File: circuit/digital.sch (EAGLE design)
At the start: 77 parts, among them IC1 OP07C, IC2 74HC4052D, IC3 AD8603UJ, IC4 AD8221R, IC5 AD8221R, IC6 LM258, IC7 LM258

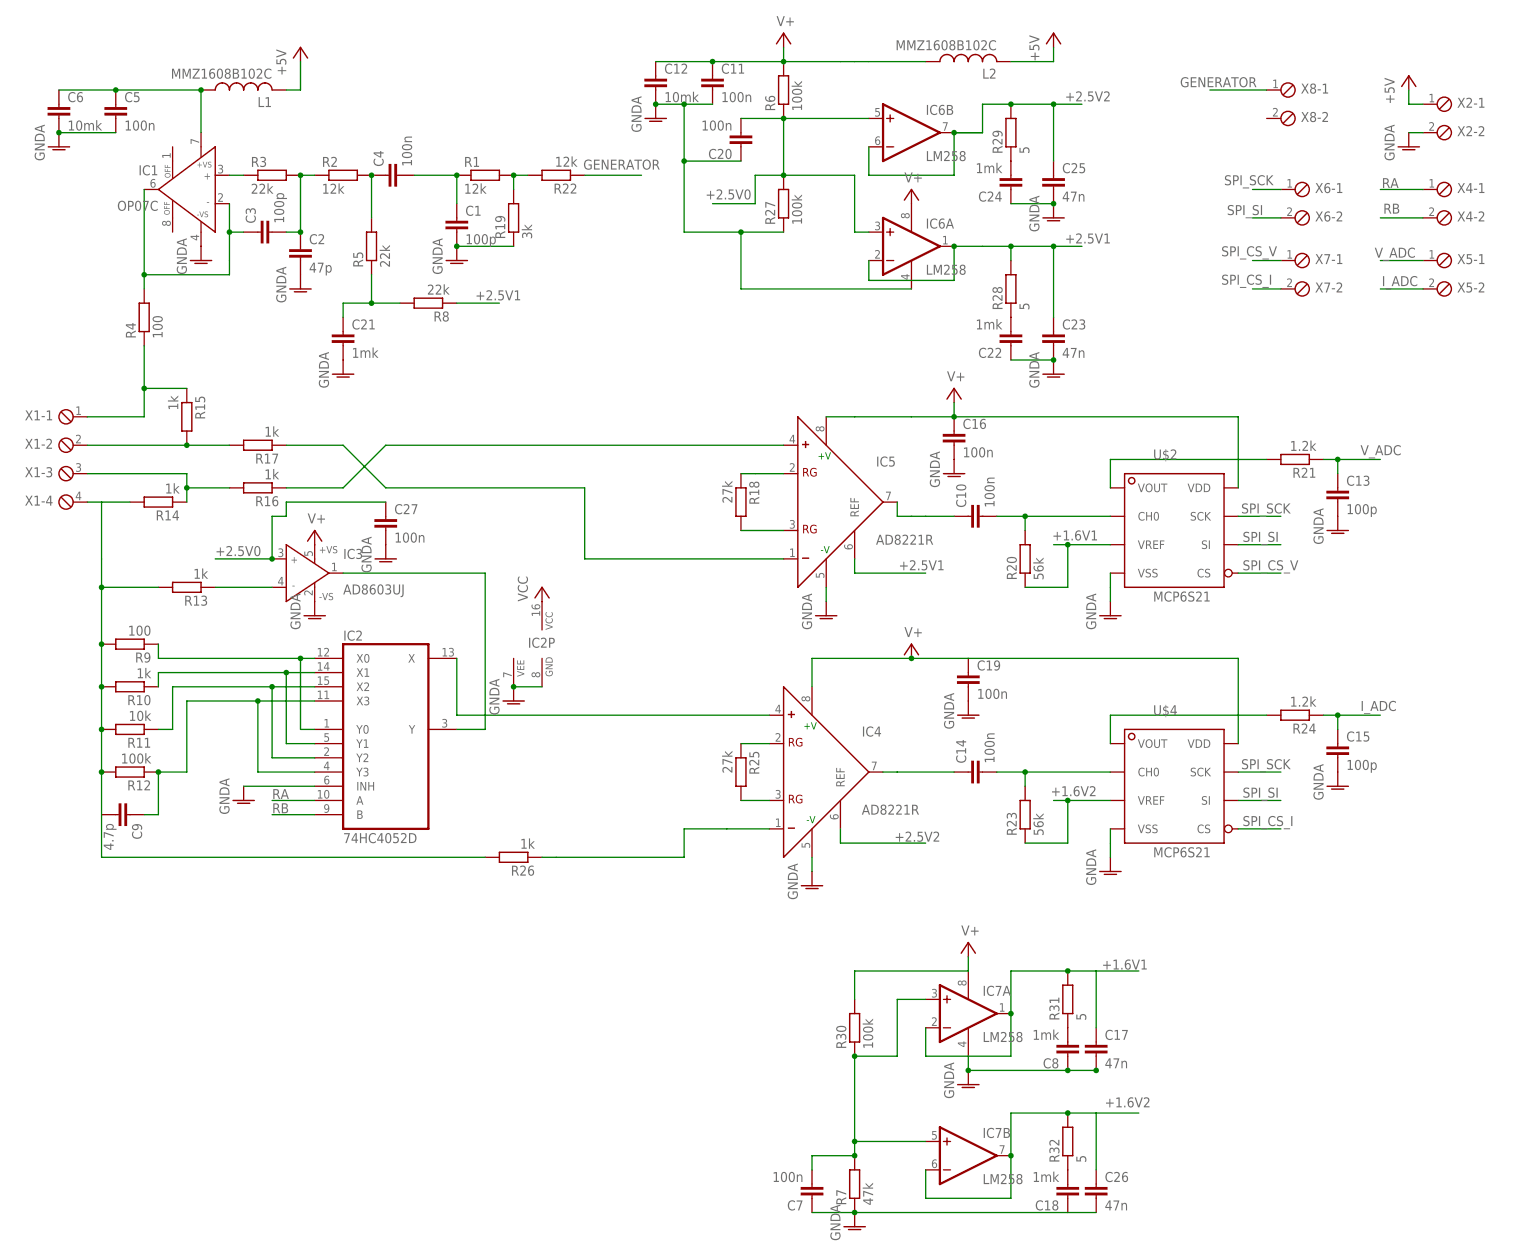
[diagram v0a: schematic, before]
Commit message: - начали делать цифровую часть
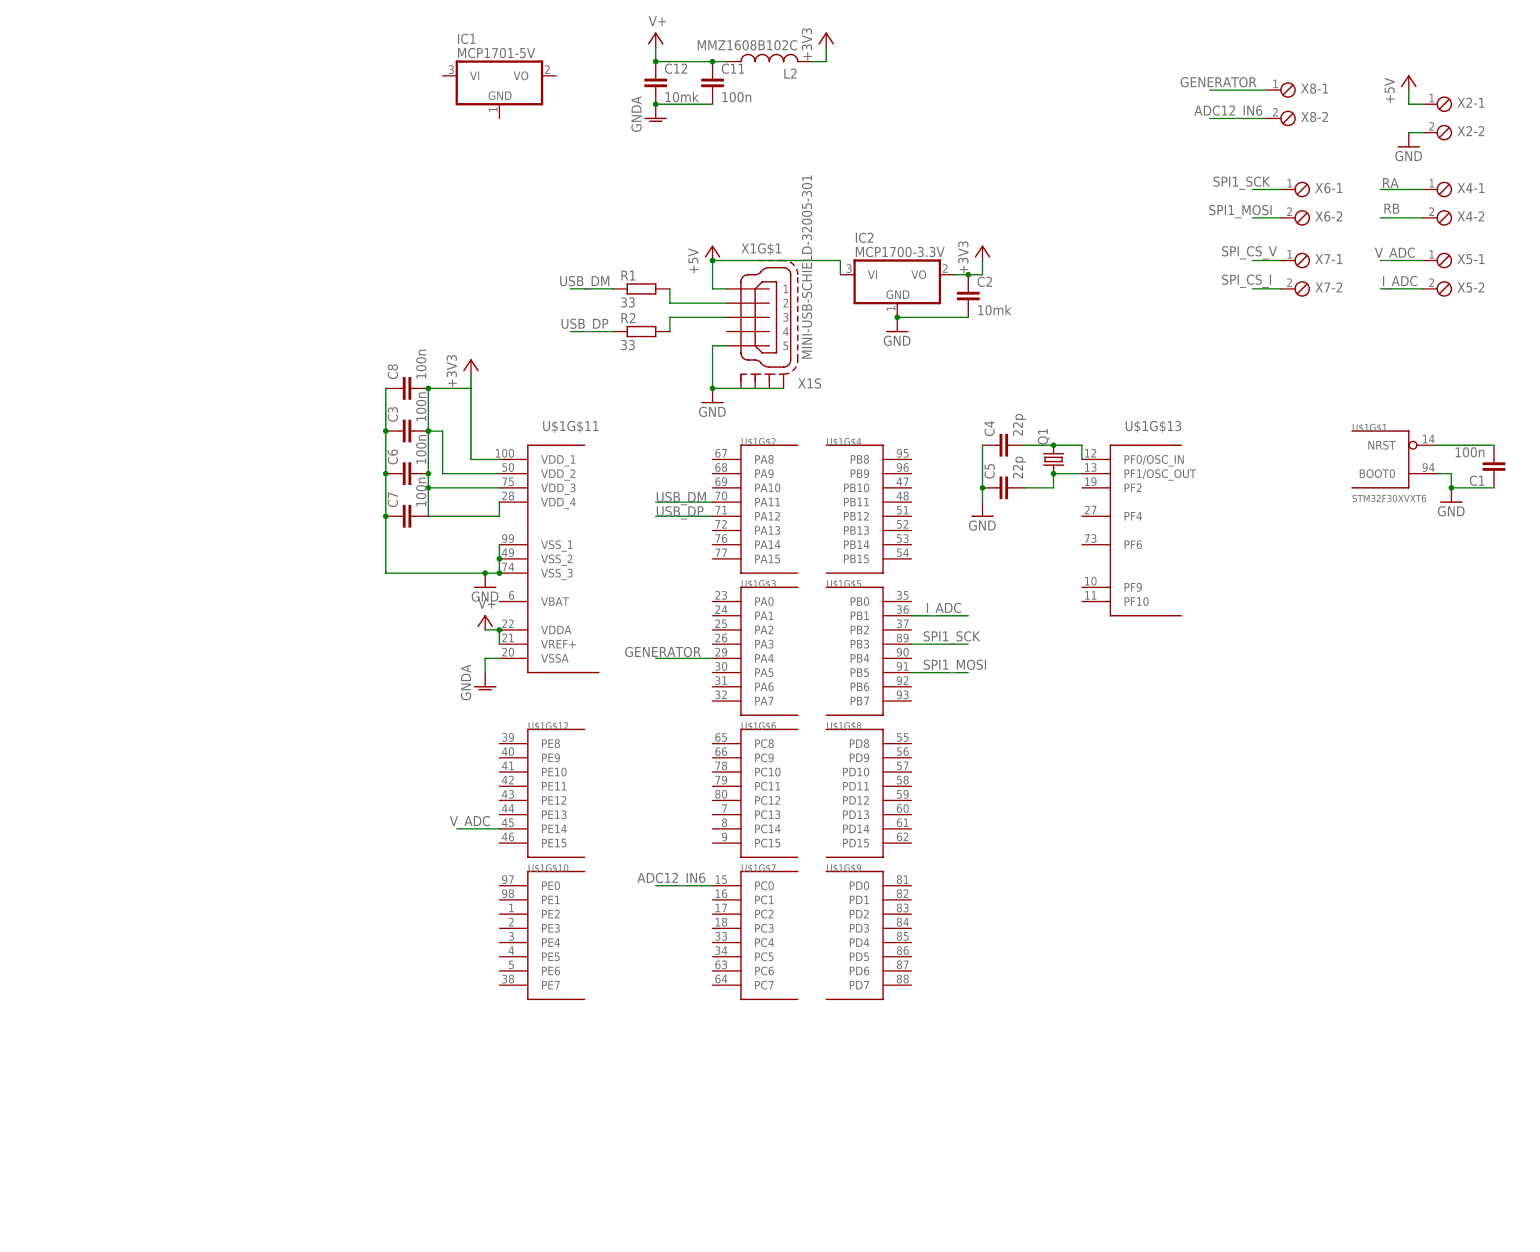
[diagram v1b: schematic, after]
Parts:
- removed C10, C14, C16, C19, C20, C27: 100n, rcl:C-EUC0603
- removed C13, C15: 100p, rcl:C-EUC0805
- removed C17, C23, C25, C26: 47n, rcl:C-EUC0805
- removed C18, C21, C22, C24: 1mk, rcl:C-EUC0603
- removed C9: 4.7p, rcl:C-EUC0805
- removed IC3: AD8603UJ, analog-devices:AD8603UJ
- removed IC4, IC5: AD8221R, balmer:AD8221R
- removed IC6, IC7: LM258, linear:LM358D
- removed L1: MMZ1608B102C, rcl:L-US
- removed R10, R13, R14, R15, R16, R17, R26: 1k, rcl:R-EU_R0603
- removed R11: 10k, rcl:R-EU_R0603
- removed R12, R27, R30, R6: 100k, rcl:R-EU_R0603
- removed R18, R25: 27k, rcl:R-EU_R0603
- removed R19: 3k, rcl:R-EU_R0603
- removed R20, R23: 56k, rcl:R-EU_R0603
- removed R21, R24: 1.2k, rcl:R-EU_R0603
- removed R22: 12k, rcl:R-EU_R0603
- removed R28, R29, R31, R32: 5, rcl:R-EU_R0805
- removed R3, R5, R8: 22k, rcl:R-EU_R0603
- removed R4, R9: 100, rcl:R-EU_R0603
- removed R7: 47k, rcl:R-EU_R0603
- removed U$2, U$4: MCP6S21, balmer:MCP6S21
- added Q1: (no value), crystal:CRYSTALHC49UP
- added U$1: STM32F30XVXT6, stm32:STM32F30XVXT6
- C1, C3: value 100p -> 100n; device rcl:C-EUC0805 -> rcl:C-EUC0603
- C2: value 47p -> 10mk
- C4, C5: value 100n -> 22p; device rcl:C-EUC0603 -> rcl:C-EUC0805
- C6: value 10mk -> 100n; device rcl:C-EUC0805 -> rcl:C-EUC0603
- C8: value 1mk -> 100n
- IC1: value OP07C -> MCP1701-5V; device analog-devices:AD817 -> linear:MCP1703CB
- IC2: value 74HC4052D -> MCP1700-3.3V; device 40xx:4052D -> linear:MCP1703CB
- L2: device rcl:L-US -> rcl:L-US0204/7
- R1, R2: value 12k -> 33
- X1: value (none) -> MINI-USB-SCHIELD-32005-301; device con-phoenix-254:MPT4 -> con-cypressindustries:MINI-USB-SCHIELD-32005-301
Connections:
- removed net +1.6V1: C17.1, IC7A.-IN, IC7A.OUT, R20.1, R31.2, U$2.VREF
- removed net +1.6V2: C26.1, IC7B.-IN, IC7B.OUT, R23.1, R32.2, U$4.VREF
- removed net +2.5V0: C20.2, C27.1, IC3.IN+, IC6A.+IN, IC6B.+IN, R27.2, R6.1
- removed net +2.5V1: C23.1, IC5.REF, IC6A.-IN, IC6A.OUT, R28.2, R8.1
- removed net +2.5V2: C25.1, IC4.REF, IC6B.-IN, IC6B.OUT, R29.2
- removed net N$10: C21.1, R5.1, R8.2
- removed net N$11: IC2A.Y, IC3.OUT
- removed net N$12: IC2A.X0, IC2A.Y0, R9.1
- removed net N$13: IC2A.X1, IC2A.Y1, R10.1
- removed net N$14: IC2A.X2, IC2A.Y2, R11.1
- removed net N$15: C9.1, IC2A.X3, IC2A.Y3, R12.1
- removed net N$16: R14.1, R16.2, X1-3.1
- removed net N$17: R15.2, R17.2, X1-2.1
- removed net N$18: C9.2, R10.2, R11.2, R12.2, R13.2, R14.2, R26.2, R9.2, X1-4.1
- removed net N$19: R15.1, R4.1, X1-1.1
- removed net N$20: C10.1, IC5.OUT
- removed net N$21: IC4.RG@1, R25.1
- removed net N$22: IC4.-, R26.1
- removed net N$23: IC5.RG@2, R18.2
- removed net N$24: IC5.RG@1, R18.1
- removed net N$25: C14.2, R23.2, U$4.CH0
- removed net N$26: R24.2, U$4.VOUT
- removed net N$27: C10.2, R20.2, U$2.CH0
- removed net N$28: R21.2, U$2.VOUT
- removed net N$29: C14.1, IC4.OUT
- removed net N$30: IC2A.X, IC4.+
- removed net N$31: C24.2, R29.1
- removed net N$32: IC5.+, R16.1
- removed net N$33: C8.2, R31.1
- removed net N$34: R1.2, R19.2, R22.2
- removed net N$35: C18.2, R32.1
- removed net N$36: C22.2, R28.1
- removed net N$41: C7.2, IC7A.+IN, IC7B.+IN, R30.1, R7.2
- removed net N$6: IC1.IN+, R3.1
- removed net N$7: C5.1, C6.1, IC1.+VS, L1.1
- removed net N$8: IC3.IN-, R13.1
- removed net N$9: IC4.RG@2, R25.2
- removed net SPI_SCK: U$2.SCK, U$4.SCK, X6-1.1
- removed net SPI_SI: U$2.SI, U$4.SI, X6-2.1
- removed net VCC: IC2P.VCC
- new net +3V3: C2.1, C3.2, C6.2, C7.2, C8.2, IC2.VO, L2.2, U$1G$11.VDD_1, U$1G$11.VDD_2, U$1G$11.VDD_3, U$1G$11.VDD_4
- new net ADC12_IN6: U$1G$7.PC0, X8-2.1
- new net GND: C1.1, C2.2, C3.1, C4.1, C5.1, C6.1, C7.1, C8.1, IC2.GND, U$1G$1.BOOT0, U$1G$11.VSS_1, U$1G$11.VSS_2, U$1G$11.VSS_3, X1G$1.5, X1S.S1, X1S.S2, X1S.S3, X1S.S4, X2-2.1
- new net SPI1_MOSI: U$1G$5.PB5, X6-2.1
- new net SPI1_SCK: U$1G$5.PB3, X6-1.1
- new net USB_DM: R1.1, U$1G$2.PA11
- new net USB_DP: R2.1, U$1G$2.PA12
- net +5V: now also IC2.VI, X1G$1.1; no longer L1.2, L2.2
- net GENERATOR: now also U$1G$3.PA4; no longer R22.1
- net GNDA: now also U$1G$11.VSSA; no longer C1.2, C13.2, C15.2, C16.2, C17.2, C18.1, C19.2, C2.2, C20.1, C21.2, C22.1, C23.2, C24.1, C25.2, C26.2, C27.2, C5.2, C6.2, C7.1, C8.1, IC1.-VS, IC2A.INH, IC2P.GND, IC2P.VEE, IC3.-VS, IC4.-V, IC5.-V, IC6P.V-, IC7P.V-, R19.1, R27.1, R7.1, U$2.VSS, U$4.VSS, X2-2.1
- net I_ADC: now also U$1G$5.PB1; no longer C15.1, R24.1
- net N$1: now also R1.2, X1G$1.2; no longer IC5.-, R17.1
- net N$2: now also R2.2, X1G$1.3; no longer C1.1, C4.2, R1.1
- net N$3: now also C1.2, U$1G$1.NRST; no longer C2.1, C3.2, R2.1, R3.2
- net N$4: now also C4.2, Q1.2, U$1G$13.PF0/OSC_IN; no longer C4.1, R2.2, R5.2
- net N$5: now also C5.2, Q1.1, U$1G$13.PF1/OSC_OUT; no longer C3.1, IC1.IN-, IC1.OUT, R4.2
- net RA: no longer IC2A.A
- net RB: no longer IC2A.B
- net SPI_CS_I: no longer U$4.CS
- net SPI_CS_V: no longer U$2.CS
- net V+: now also U$1G$11.VDDA, U$1G$11.VREF+; no longer C16.1, C19.1, IC3.+VS, IC4.+V, IC5.+V, IC6P.V+, IC7P.V+, R30.2, R6.2, U$2.VDD, U$4.VDD
- net V_ADC: now also U$1G$12.PE14; no longer C13.1, R21.1
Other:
- moved on the sheet: C1, C2, C3, C4, C5, C6, C7, C8, L2, R1, R2

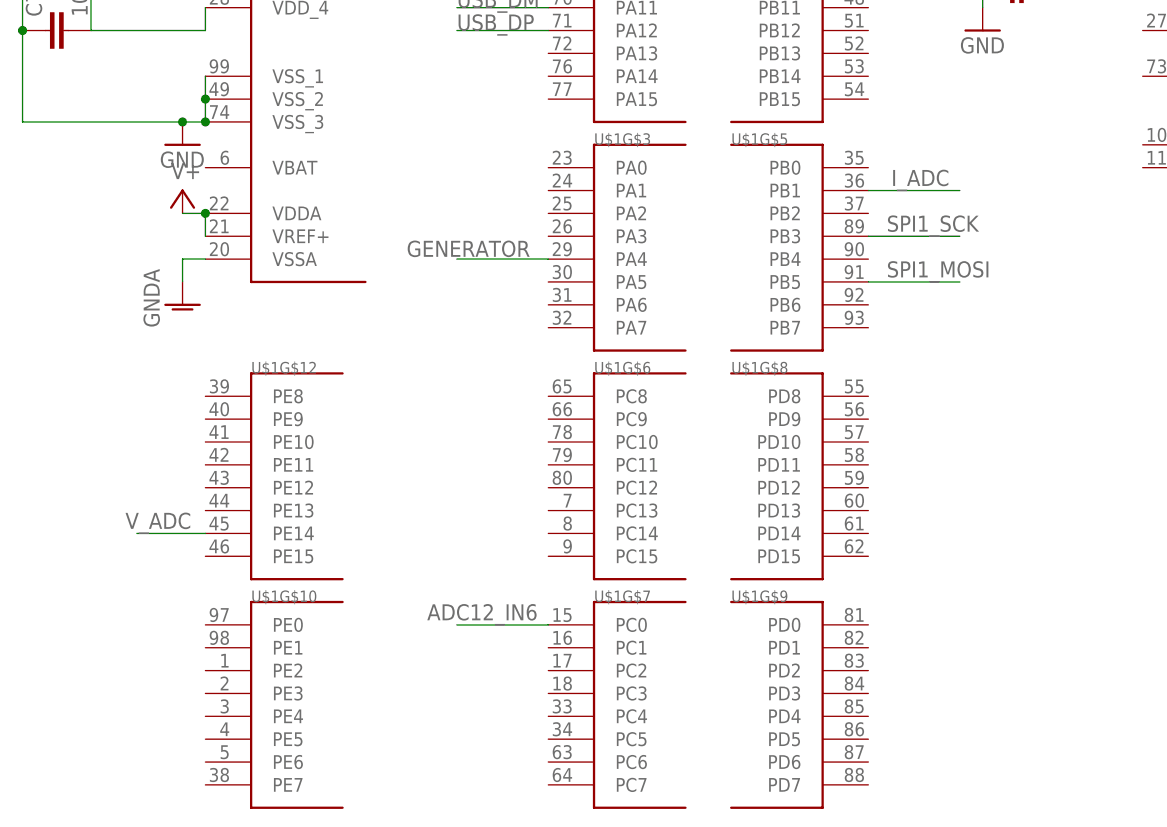
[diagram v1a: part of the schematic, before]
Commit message: - развели все пины идущие к аналоговой части
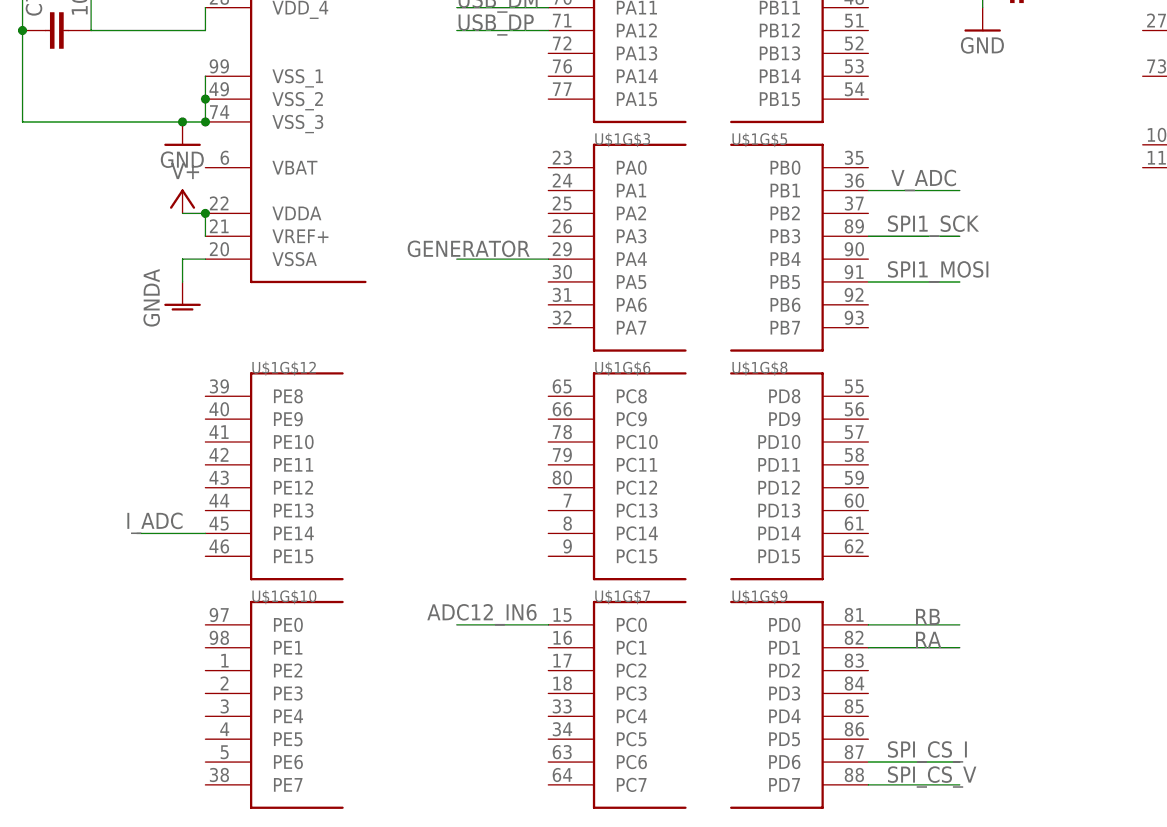
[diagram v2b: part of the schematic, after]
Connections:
- net I_ADC: now also U$1G$12.PE14; no longer U$1G$5.PB1
- net RA: now also U$1G$9.PD1
- net RB: now also U$1G$9.PD0
- net SPI_CS_I: now also U$1G$9.PD6
- net SPI_CS_V: now also U$1G$9.PD7
- net V_ADC: now also U$1G$5.PB1; no longer U$1G$12.PE14
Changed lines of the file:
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@@
 </segment>
 <segment>
-<pinref part="U$1" gate="G$12" pin="PE14"/>
-<wire x1="12.7" y1="-38.1" x2="5.08" y2="-38.1" width="0.1524" layer="91"/>
-<label x="3.81" y="-37.592" size="1.778" layer="95"/>
+<pinref part="U$1" gate="G$5" pin="PB1"/>
+<wire x1="86.36" y1="0" x2="96.52" y2="0" width="0.1524" layer="91"/>
+<label x="88.9" y="0.508" size="1.778" layer="95"/>
 </segment>
 </net>
@@
 <label x="170.434" y="76.454" size="1.778" layer="95"/>
 </segment>
+<segment>
+<pinref part="U$1" gate="G$9" pin="PD1"/>
+<wire x1="86.36" y1="-50.8" x2="96.52" y2="-50.8" width="0.1524" layer="91"/>
+<label x="91.44" y="-50.8" size="1.778" layer="95"/>
+</segment>
 </net>
 <net name="RB" class="0">
@@
 <label x="170.688" y="71.882" size="1.778" layer="95"/>
 </segment>
+<segment>
+<pinref part="U$1" gate="G$9" pin="PD0"/>
+<wire x1="86.36" y1="-48.26" x2="96.52" y2="-48.26" width="0.1524" layer="91"/>
+<label x="91.44" y="-48.26" size="1.778" layer="95"/>
+</segment>
 </net>
 <net name="SPI_CS_I" class="0">
@@
 <wire x1="152.4" y1="58.42" x2="147.32" y2="58.42" width="0.1524" layer="91"/>
 <label x="141.732" y="59.182" size="1.778" layer="95"/>
+</segment>
+<segment>
+<pinref part="U$1" gate="G$9" pin="PD6"/>
+<wire x1="86.36" y1="-63.5" x2="96.52" y2="-63.5" width="0.1524" layer="91"/>
+<label x="88.392" y="-62.992" size="1.778" layer="95"/>
 </segment>
 </net>
@@
 </segment>
 <segment>
-<pinref part="U$1" gate="G$5" pin="PB1"/>
-<wire x1="86.36" y1="0" x2="96.52" y2="0" width="0.1524" layer="91"/>
-<label x="88.9" y="0.508" size="1.778" layer="95"/>
+<pinref part="U$1" gate="G$12" pin="PE14"/>
+<wire x1="12.7" y1="-38.1" x2="5.08" y2="-38.1" width="0.1524" layer="91"/>
+<label x="3.81" y="-37.592" size="1.778" layer="95"/>
 </segment>
 </net>
@@
 <label x="141.732" y="64.262" size="1.778" layer="95"/>
 </segment>
+<segment>
+<pinref part="U$1" gate="G$9" pin="PD7"/>
+<wire x1="86.36" y1="-66.04" x2="96.52" y2="-66.04" width="0.1524" layer="91"/>
+<label x="88.392" y="-65.786" size="1.778" layer="95"/>
+</segment>
 </net>

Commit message: - все кроме LCD дисплея
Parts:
- added C10, C9: 1mk, rcl:C-EUC0603
- added R3: 0, rcl:R-EU_R0603
- added X3: (no value), con-phoenix-254:MPT2
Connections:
- new net N$7: C9.1, IC1.VI, X3-1.1
- net +5V: now also C10.1, IC1.VO
- net GND: now also C10.2, C9.2, IC1.GND, R3.2, X3-2.1
- net GNDA: now also R3.1
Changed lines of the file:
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@@
 <part name="C8" library="rcl" deviceset="C-EU" device="C0603" value="100n"/>
 <part name="+3V3" library="supply1" deviceset="+3V3" device=""/>
+<part name="X3" library="con-phoenix-254" deviceset="MPT2" device=""/>
+<part name="GND8" library="supply1" deviceset="GND" device=""/>
+<part name="GND9" library="supply1" deviceset="GNDA" device=""/>
+<part name="R3" library="rcl" deviceset="R-EU_" device="R0603" value="0"/>
+<part name="GND11" library="supply1" deviceset="GND" device=""/>
+<part name="C9" library="rcl" deviceset="C-EU" device="C0603" value="1mk"/>
+<part name="C10" library="rcl" deviceset="C-EU" device="C0603" value="1mk"/>
+<part name="P+2" library="supply1" deviceset="+5V" device=""/>
 </parts>
 <sheets>
@@
 <instance part="C8" gate="G$1" x="-5.08" y="40.64" rot="R90"/>
 <instance part="+3V3" gate="G$1" x="7.62" y="45.72"/>
+<instance part="X3" gate="-1" x="-12.7" y="93.98" rot="MR0"/>
+<instance part="X3" gate="-2" x="-12.7" y="88.9" rot="MR0"/>
+<instance part="GND8" gate="1" x="116.84" y="88.9"/>
+<instance part="GND9" gate="1" x="101.6" y="88.9"/>
+<instance part="R3" gate="G$1" x="109.22" y="91.44"/>
+<instance part="GND11" gate="1" x="12.7" y="86.36"/>
+<instance part="C9" gate="G$1" x="-2.54" y="93.98"/>
+<instance part="C10" gate="G$1" x="25.4" y="93.98"/>
+<instance part="P+2" gate="1" x="25.4" y="104.14"/>
 </instances>
 <busses>
@@
 <junction x="50.8" y="63.5"/>
 </segment>
+<segment>
+<pinref part="IC1" gate="G$1" pin="VO"/>
+<wire x1="25.4" y1="96.52" x2="22.86" y2="96.52" width="0.1524" layer="91"/>
+<pinref part="C10" gate="G$1" pin="1"/>
+<pinref part="P+2" gate="1" pin="+5V"/>
+<wire x1="25.4" y1="96.52" x2="25.4" y2="101.6" width="0.1524" layer="91"/>
+<junction x="25.4" y="96.52"/>
+</segment>
 </net>
 <net name="GNDA" class="0">
@@
 <wire x1="12.7" y1="-7.62" x2="10.16" y2="-7.62" width="0.1524" layer="91"/>
 <wire x1="10.16" y1="-7.62" x2="10.16" y2="-10.16" width="0.1524" layer="91"/>
+</segment>
+<segment>
+<pinref part="GND9" gate="1" pin="GNDA"/>
+<pinref part="R3" gate="G$1" pin="1"/>
+<wire x1="101.6" y1="91.44" x2="104.14" y2="91.44" width="0.1524" layer="91"/>
 </segment>
 </net>
@@
 <junction x="-7.62" y="25.4"/>
 <junction x="-7.62" y="33.02"/>
+</segment>
+<segment>
+<pinref part="GND8" gate="1" pin="GND"/>
+<pinref part="R3" gate="G$1" pin="2"/>
+<wire x1="116.84" y1="91.44" x2="114.3" y2="91.44" width="0.1524" layer="91"/>
+</segment>
+<segment>
+<pinref part="IC1" gate="G$1" pin="GND"/>
+<pinref part="GND11" gate="1" pin="GND"/>
+<wire x1="25.4" y1="88.9" x2="12.7" y2="88.9" width="0.1524" layer="91"/>
+<pinref part="C9" gate="G$1" pin="2"/>
+<wire x1="-2.54" y1="88.9" x2="12.7" y2="88.9" width="0.1524" layer="91"/>
+<pinref part="C10" gate="G$1" pin="2"/>
+<pinref part="X3" gate="-2" pin="1"/>
+<wire x1="-10.16" y1="88.9" x2="-2.54" y2="88.9" width="0.1524" layer="91"/>
+<junction x="12.7" y="88.9"/>
+<junction x="-2.54" y="88.9"/>
 </segment>
 </net>
@@
 </segment>
 </net>
+<net name="N$7" class="0">
+<segment>
+<pinref part="C9" gate="G$1" pin="1"/>
+<pinref part="IC1" gate="G$1" pin="VI"/>
+<wire x1="-2.54" y1="96.52" x2="2.54" y2="96.52" width="0.1524" layer="91"/>
+<pinref part="X3" gate="-1" pin="1"/>
+<wire x1="-10.16" y1="93.98" x2="-10.16" y2="96.52" width="0.1524" layer="91"/>
+<wire x1="-10.16" y1="96.52" x2="-2.54" y2="96.52" width="0.1524" layer="91"/>
+<junction x="-2.54" y="96.52"/>
+</segment>
+</net>
